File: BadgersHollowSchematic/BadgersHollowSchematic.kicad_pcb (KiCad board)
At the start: 2 copper layers, 108.2 x 119.1 mm, 109 parts, among them J1 usbc_gct, J2 AVR-ISP-6, SW1 SW_Push, SW10 SW_SPST, SW11 SW_SPST, SW12 SW_SPST, SW13 SW_SPST, SW14 SW_SPST, SW15 SW_SPST, SW17 SW_SPST, SW18 SW_SPST, SW19 SW_SPST, SW2 SW_Push, SW20 SW_SPST, SW21 SW_SPST, SW22 SW_SPST, SW23 SW_SPST, SW24 SW_SPST, SW25 SW_SPST, SW26 SW_SPST, SW27 Rotory Encoder, SW3 SW_SPST, SW4 SW_SPST, SW5 SW_SPST, SW6 SW_SPST, SW7 SW_SPST, SW8 SW_SPST, SW9 SW_SPST, U1 ATmega32U4-AU, Y1 Crystal

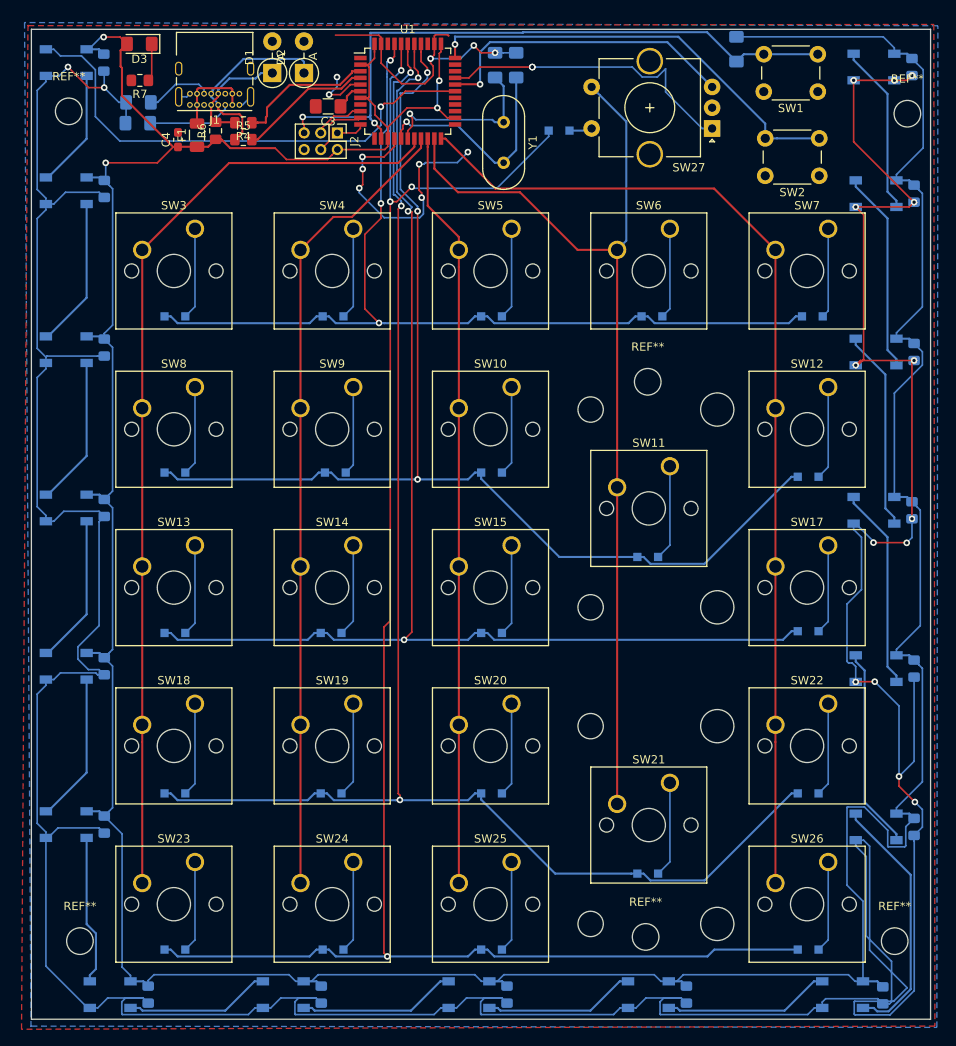
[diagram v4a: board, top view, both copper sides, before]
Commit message: Updated usbb differential track lengths
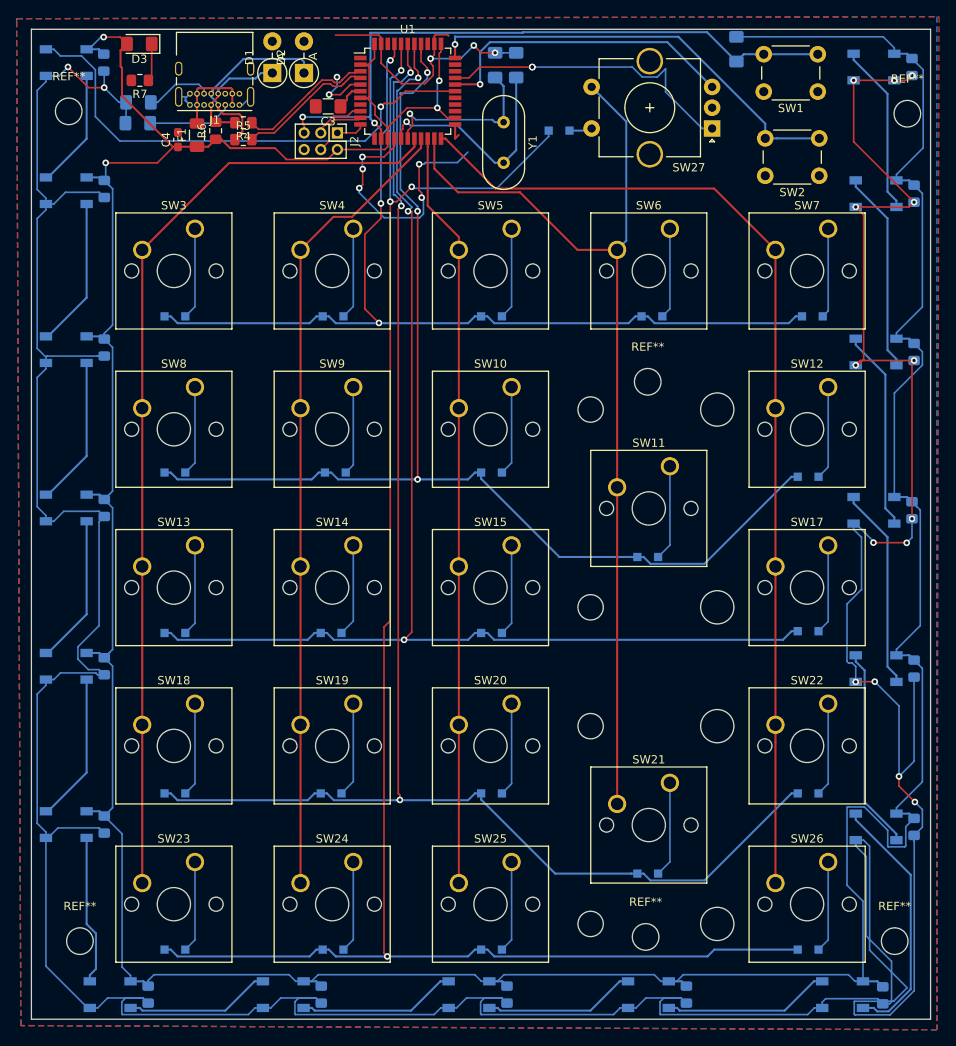
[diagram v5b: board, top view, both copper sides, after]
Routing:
- net GND: track 607.6 -> 611.2 mm, vias 27 -> 26
